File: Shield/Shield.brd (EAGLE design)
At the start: 174 x 56 mm, 15 parts

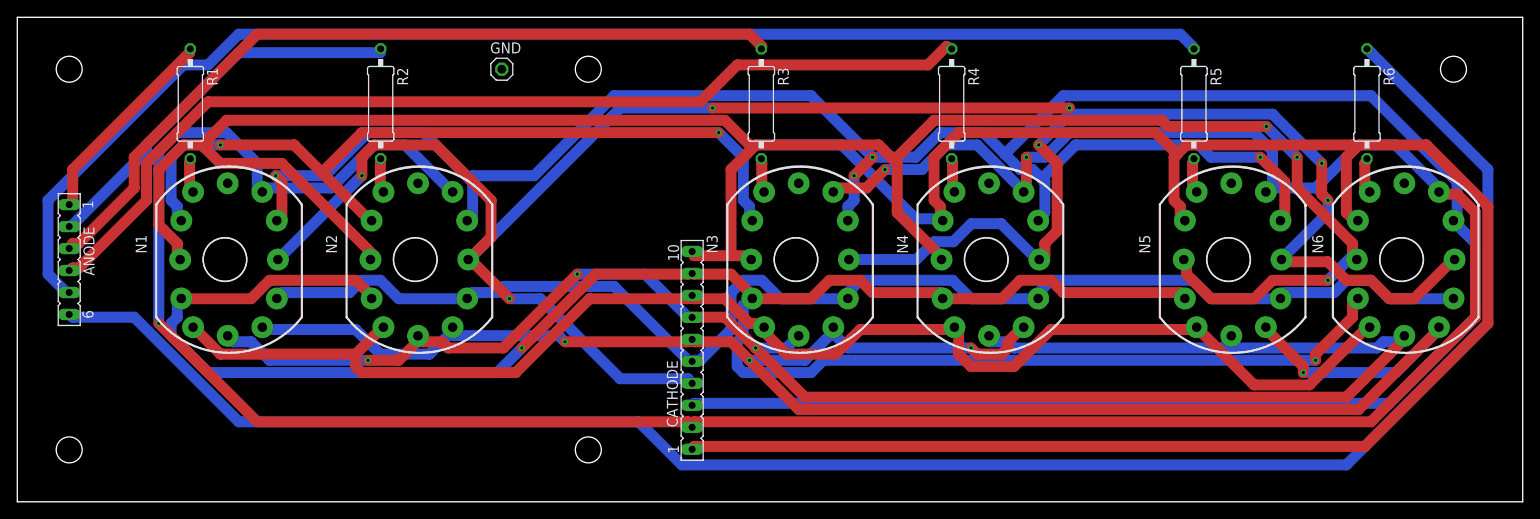
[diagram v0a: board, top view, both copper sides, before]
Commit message: spaced routes out
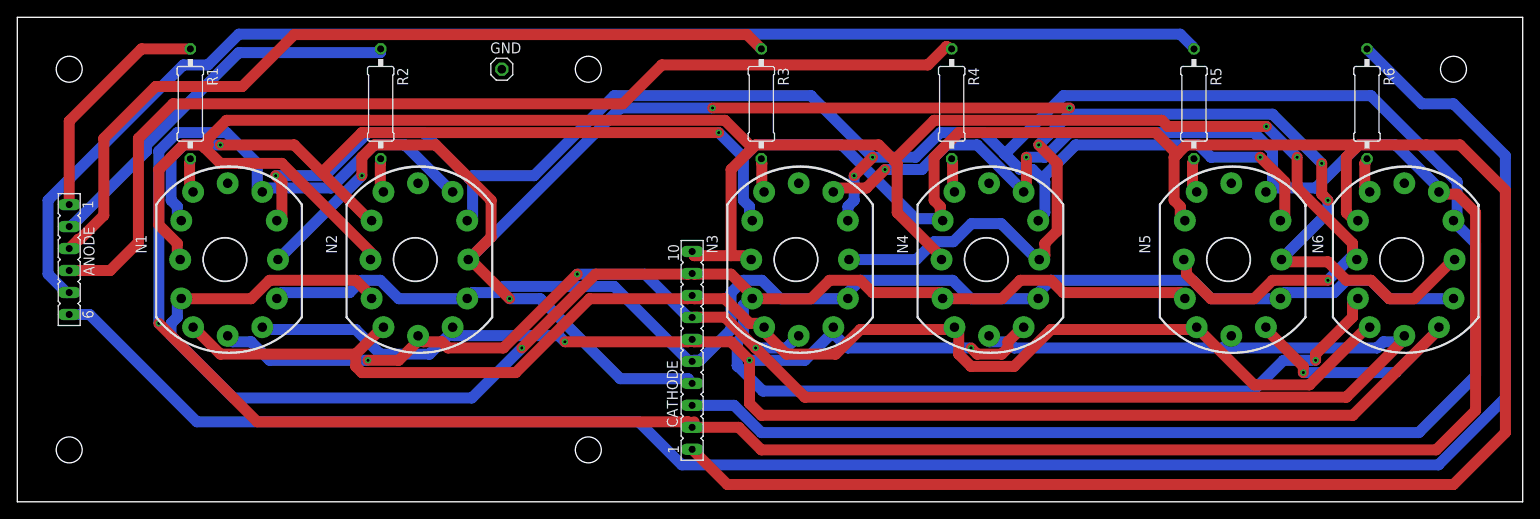
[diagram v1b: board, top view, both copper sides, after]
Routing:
- net 0: track 329.4 -> 345.2 mm
- net N$2: track 215.5 -> 225.5 mm
- net 1: track 335.1 -> 344.1 mm
- net 2: track 335.5 -> 342.0 mm
- net N$6: track 115.3 -> 119.8 mm
- net 8: track 243.6 -> 247.8 mm
- net 5: track 209.8 -> 213.3 mm
- net N$1: track 23.7 -> 27.1 mm
- net N$5: track 93.3 -> 96.1 mm

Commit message: forgot to save before commit... Comment: See last commit
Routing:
- net 9: track 251.5 -> 392.1 mm, vias 3 -> 10
- net 7: track 162.7 -> 298.3 mm, vias 0 -> 2
- net 1: track 344.1 -> 253.7 mm, vias 3 -> 8
- net 4: track 155.2 -> 229.5 mm, vias 0 -> 8
- net 0: track 345.2 -> 299.0 mm, vias 2 -> 10
- net N$2: track 225.5 -> 179.3 mm
- net 8: track 247.8 -> 291.8 mm, vias 2 -> 9
- net 2: track 342.0 -> 306.3 mm, vias 4 -> 10
- net 5: track 213.3 -> 178.5 mm, vias 4 -> 0
- net 3: track 265.5 -> 253.2 mm, vias 7 -> 4
- net N$4: track 45.1 -> 52.8 mm, vias 0 -> 2
- net N$3: track 153.0 -> 148.5 mm, vias 0 -> 2
- net N$6: track 119.8 -> 124.2 mm, vias 0 -> 4
- net N$1: track 27.1 -> 23.8 mm
- net 6: track 208.6 -> 207.3 mm, vias 3 -> 9
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- added copper zone on layer 16, net GND
- added copper zone on layer 1, net N$8

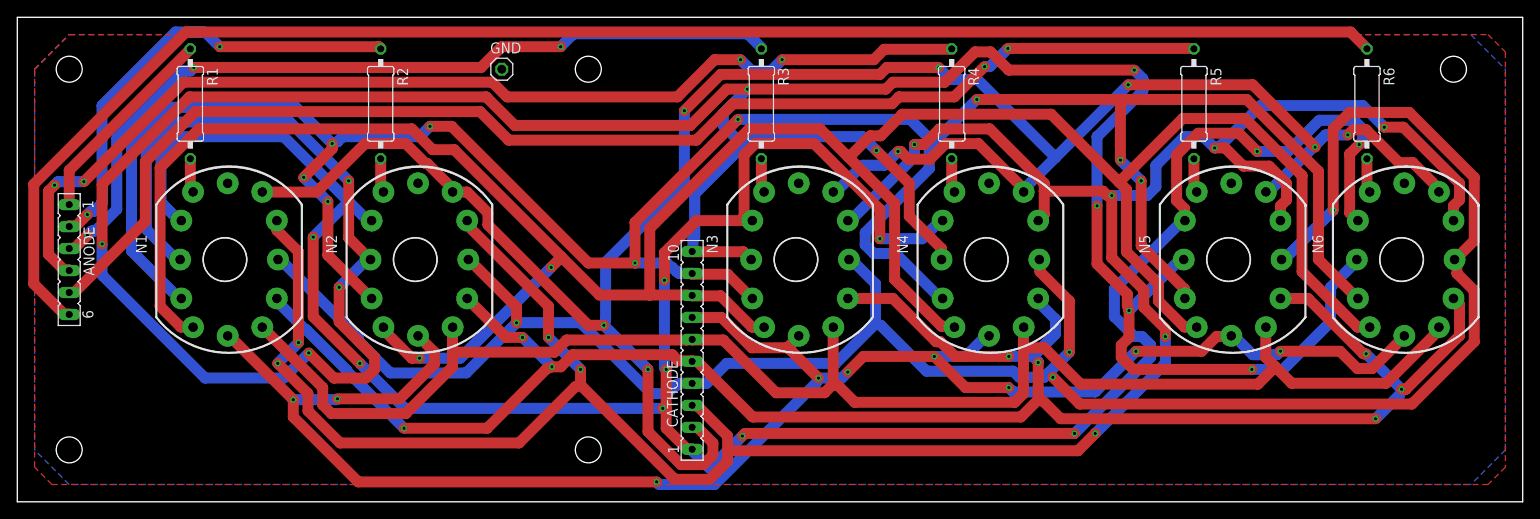
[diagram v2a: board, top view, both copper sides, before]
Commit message: applied rules to shield
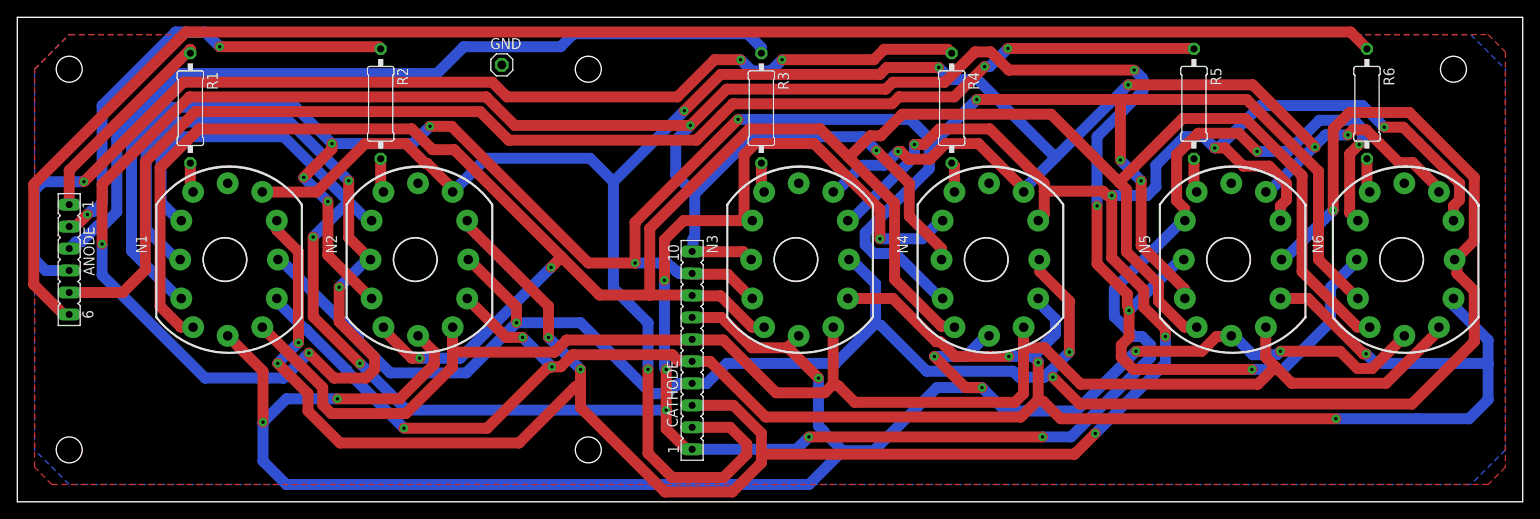
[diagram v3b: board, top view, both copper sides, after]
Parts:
- moved GND 0.50 mm to (56.0, 50.5)
- moved R1 0.50 mm to (20.0, 45.5)
- moved R3 0.50 mm to (86.0, 45.5)
- moved R4 0.50 mm to (108.0, 45.5)
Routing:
- net 6: track 207.3 -> 232.3 mm, vias 9 -> 7
- net 4: track 229.5 -> 247.7 mm, vias 8 -> 7
- net 2: track 306.3 -> 313.4 mm
- net 1: track 253.7 -> 259.9 mm, vias 8 -> 7
- net N$6: track 124.2 -> 128.6 mm, vias 4 -> 3
- net N$3: track 148.5 -> 151.8 mm
- net 8: track 291.8 -> 294.0 mm
- net 0: track 299.0 -> 298.1 mm
- net 9: track 392.1 -> 393.0 mm
- net N$5: track 95.9 -> 96.6 mm, vias 3 -> 0
- net N$9: track 3.96 -> 3.46 mm
- net N$7: track 3.96 -> 3.46 mm
